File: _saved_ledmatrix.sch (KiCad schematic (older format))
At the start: 4 parts

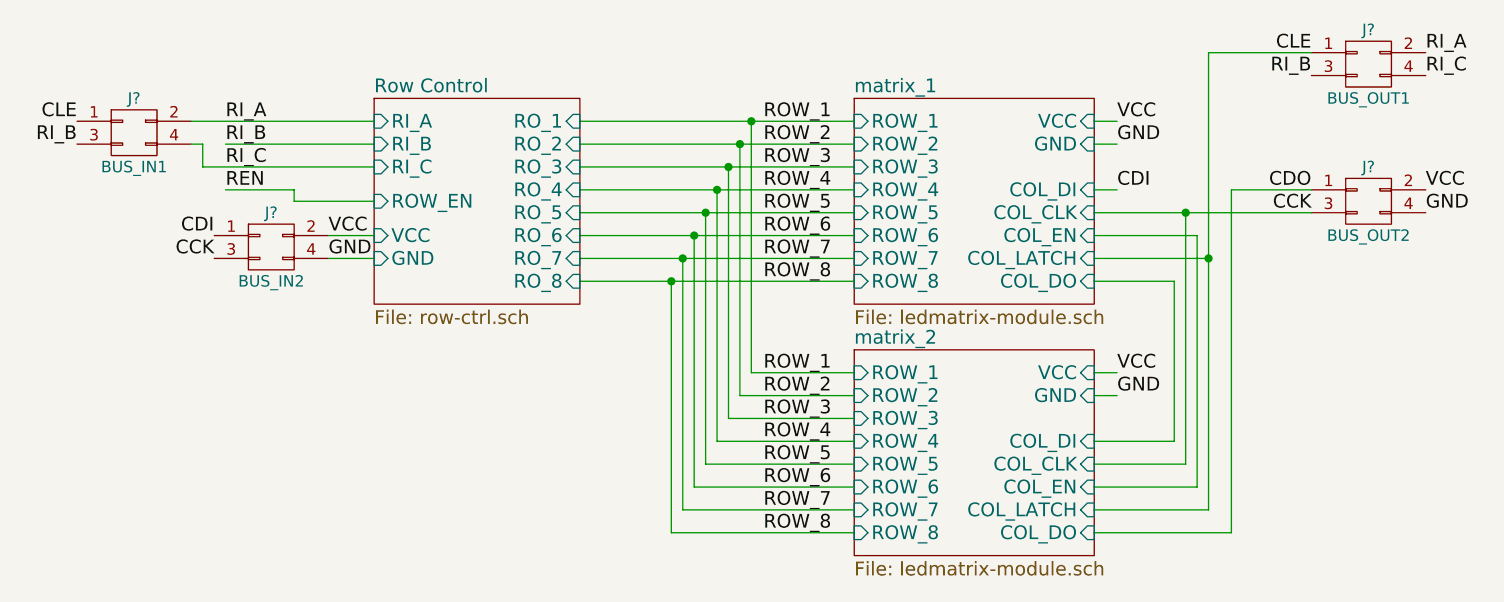
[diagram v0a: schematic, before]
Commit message: dual matrix with 2x2 interconnects
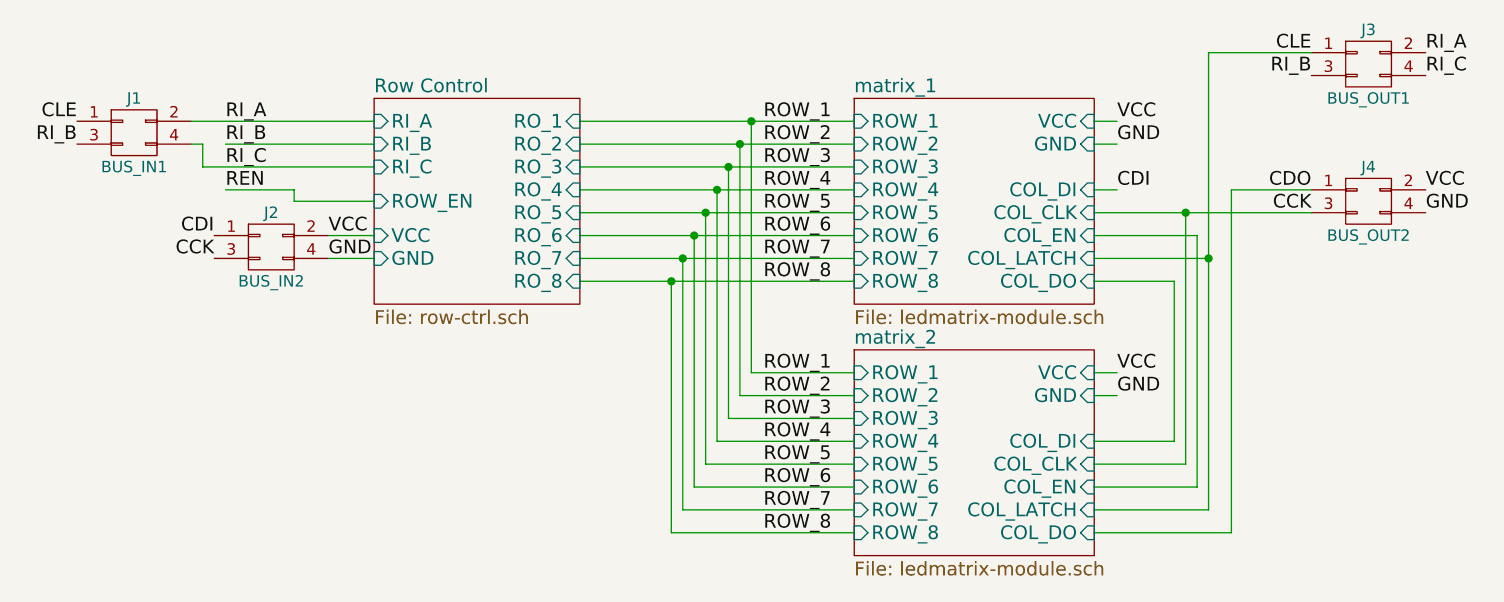
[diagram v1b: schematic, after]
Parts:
- gave numbers to parts that had none: 4
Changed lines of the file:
@@
 	6450 3000 6450 1900
 $Comp
-L CONN_02X02 J?
+L CONN_02X02 J4
 U 1 1 59AB19E8
 P 7250 1850
-F 0 "J?" H 7250 2000 50  0000 C CNN
+F 0 "J4" H 7250 2000 50  0000 C CNN
 F 1 "BUS_OUT2" H 7250 1700 50  0000 C CNN
 F 2 "" H 7250 650 50  0001 C CNN
@@
 	6500 2000 6050 2000
 $Comp
-L CONN_02X02 J?
+L CONN_02X02 J3
 U 1 1 59AB23F4
 P 7250 1250
-F 0 "J?" H 7250 1400 50  0000 C CNN
+F 0 "J3" H 7250 1400 50  0000 C CNN
 F 1 "BUS_OUT1" H 7250 1100 50  0000 C CNN
 F 2 "" H 7250 50  50  0001 C CNN
@@
 CLE
 $Comp
-L CONN_02X02 J?
+L CONN_02X02 J2
 U 1 1 59AB4B91
 P 2450 2050
-F 0 "J?" H 2450 2200 50  0000 C CNN
+F 0 "J2" H 2450 2200 50  0000 C CNN
 F 1 "BUS_IN2" H 2450 1900 50  0000 C CNN
 F 2 "" H 2450 850 50  0001 C CNN
@@
 $EndComp
 $Comp
-L CONN_02X02 J?
+L CONN_02X02 J1
 U 1 1 59AB4B97
 P 1850 1550
-F 0 "J?" H 1850 1700 50  0000 C CNN
+F 0 "J1" H 1850 1700 50  0000 C CNN
 F 1 "BUS_IN1" H 1850 1400 50  0000 C CNN
 F 2 "" H 1850 350 50  0001 C CNN
